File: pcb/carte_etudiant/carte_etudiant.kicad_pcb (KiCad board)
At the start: 2 copper layers, 70 x 77.5 mm, 3 parts, among them J1 Conn_02x15_Odd_Even, J2 Conn_01x14, U1 NUCLEO64-F103RB

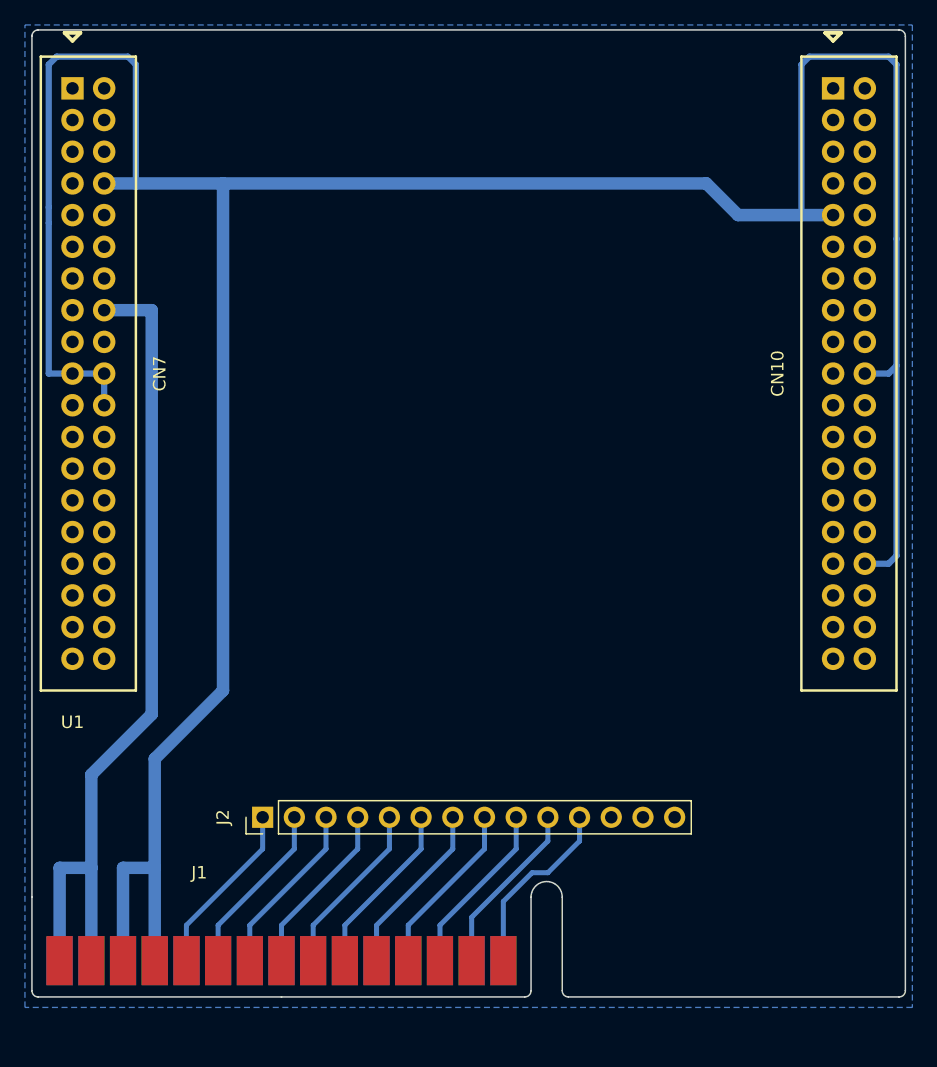
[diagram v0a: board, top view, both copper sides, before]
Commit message: deplacement du connecteur
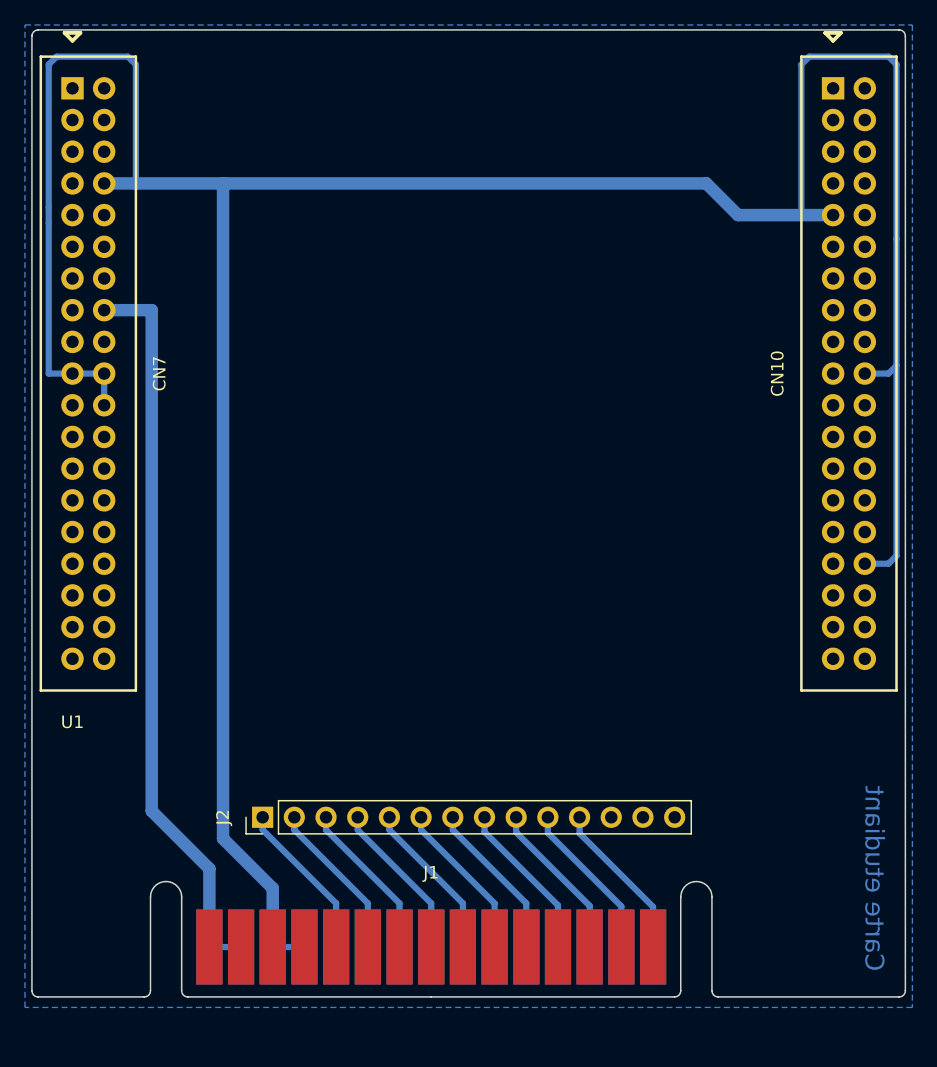
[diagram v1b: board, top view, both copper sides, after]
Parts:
- moved J1 12.0 mm to (124.0, 154.1)
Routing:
- net GND: track 248.0 -> 239.9 mm
- net +3V3: track 67.9 -> 60.4 mm
- net Net-(J1-Pad30): track 14.8 -> 12.8 mm
- net Net-(J1-Pad26): track 14.0 -> 12.8 mm
- net Net-(J1-Pad24): track 14.0 -> 12.8 mm
- net Net-(J1-Pad22): track 14.0 -> 12.8 mm
- net Net-(J1-Pad18): track 14.0 -> 12.8 mm
- net Net-(J1-Pad16): track 14.0 -> 12.8 mm
- net Net-(J1-Pad14): track 14.0 -> 12.8 mm
- net Net-(J1-Pad20): track 14.0 -> 12.8 mm
- net Net-(J1-Pad28): track 14.0 -> 12.8 mm
- net Net-(J1-Pad10): track 14.0 -> 13.0 mm
- net Net-(J1-Pad12): track 14.0 -> 13.3 mm
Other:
- outline, holes or cut-outs redrawn
- board text added: "Carte etudiant"

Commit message: * Passage d un connecteur 30 pts à un connecteur 40 pts sur la carte etudiant * Correction sur le fichier de pinout (changement du nom du signal SERVO_PWM en SERVO_VOILE_PWM)
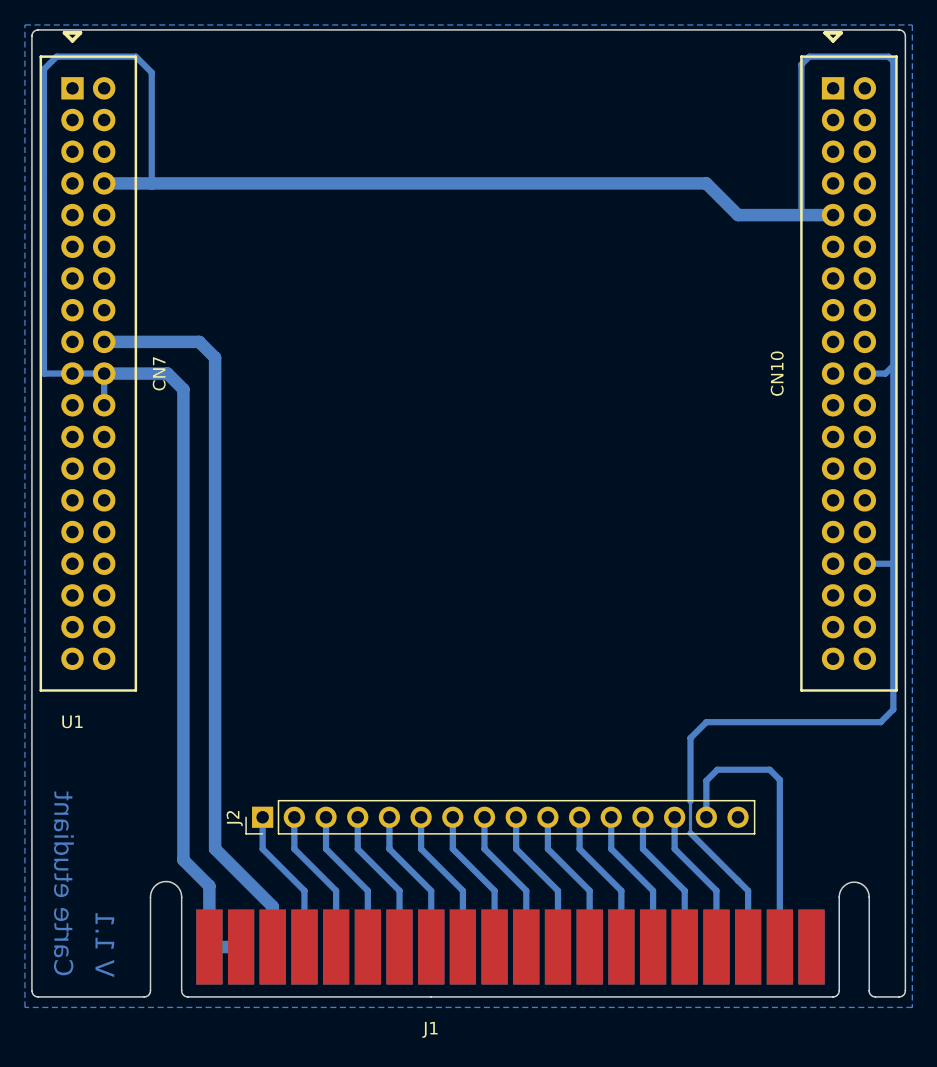
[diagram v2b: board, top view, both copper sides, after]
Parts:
- J1: footprint Insa:TE 5530841-2 PCB Edge -> Insa:5-5530843-4-PCB
- J2: footprint Connector_PinHeader_2.54mm:PinHeader_1x14_P2.54mm_Vertical -> Connector_PinHeader_2.54mm:PinHeader_1x16_P2.54mm_Vertical
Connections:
- J1 pad 10: Net-(J1-Pad10) -> /CAPTEUR_SPI_MISO
- J1 pad 12: Net-(J1-Pad12) -> /CAPTEUR_SPI_CLK
- J1 pad 14: Net-(J1-Pad14) -> /CAPTEUR_SPI_CS
- J1 pad 16: Net-(J1-Pad16) -> /PLATEAU_DIRECTION
- J1 pad 18: Net-(J1-Pad18) -> /SERVO_VOILE_PWM
- J1 pad 2: +3V3 -> GND
- J1 pad 20: Net-(J1-Pad20) -> /PLATEAU_PWM
- J1 pad 22: Net-(J1-Pad22) -> /XBEE_UART_TX
- J1 pad 24: Net-(J1-Pad24) -> /XBEE_UART_RX
- J1 pad 26: Net-(J1-Pad26) -> /CAPTEUR_I2C_SCL
- J1 pad 28: Net-(J1-Pad28) -> /CAPTEUR_I2C_SDA
- J1 pad 30: Net-(J1-Pad30) -> /GIROUETTE_PHB
- J1 pad 4: +3V3 -> GND
- J1 pad 6: GND -> +5V
- J1 pad 8: GND -> /CAPTEUR_SPI_MOSI
- J2 pad 1: Net-(J1-Pad10) -> /CAPTEUR_SPI_MOSI
- J2 pad 10: Net-(J1-Pad28) -> /CAPTEUR_I2C_SCL
- J2 pad 11: Net-(J1-Pad30) -> /CAPTEUR_I2C_SDA
- J2 pad 12: (no net) -> /GIROUETTE_PHB
- J2 pad 13: (no net) -> /GIROUETTE_PHA
- J2 pad 14: (no net) -> /GIROUETTE_INDEX
- J2 pad 2: Net-(J1-Pad12) -> /CAPTEUR_SPI_MISO
- J2 pad 3: Net-(J1-Pad14) -> /CAPTEUR_SPI_CLK
- J2 pad 4: Net-(J1-Pad16) -> /CAPTEUR_SPI_CS
- J2 pad 5: Net-(J1-Pad18) -> /PLATEAU_DIRECTION
- J2 pad 6: Net-(J1-Pad20) -> /SERVO_VOILE_PWM
- J2 pad 7: Net-(J1-Pad22) -> /PLATEAU_PWM
- J2 pad 8: Net-(J1-Pad24) -> /XBEE_UART_TX
- J2 pad 9: Net-(J1-Pad26) -> /XBEE_UART_RX
- U1 pad 16: +3V3 -> (no net)
- U1 pad 18: (no net) -> +5V
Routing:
- net +3V3: track 60.4 -> 0.00 mm
- net +5V: track 0.00 -> 58.6 mm
- net GND: track 239.9 -> 277.2 mm
- net /TENSION_BATTERIE: track 0.00 -> 22.9 mm
- net Net-(J1-Pad12): track 13.3 -> 0.00 mm
- net Net-(J1-Pad10): track 13.0 -> 0.00 mm
- net Net-(J1-Pad30): track 12.8 -> 0.00 mm
- net Net-(J1-Pad20): track 12.8 -> 0.00 mm
- net Net-(J1-Pad28): track 12.8 -> 0.00 mm
- net Net-(J1-Pad22): track 12.8 -> 0.00 mm
- net Net-(J1-Pad18): track 12.8 -> 0.00 mm
- net Net-(J1-Pad16): track 12.8 -> 0.00 mm
- net Net-(J1-Pad14): track 12.8 -> 0.00 mm
- net Net-(J1-Pad24): track 12.8 -> 0.00 mm
- net Net-(J1-Pad26): track 12.8 -> 0.00 mm
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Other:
- outline, holes or cut-outs redrawn
- board text added: "V 1.1"
